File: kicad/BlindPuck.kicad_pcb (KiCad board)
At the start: 2 copper layers, 30.5 x 50.8 mm, 9 parts, among them Q1 FQP30N06, U1 PK-21N30P-TPQ, U2 DD06AJSA, U3 PK-21N30P-TPQ, U4 FeatherHuzzah, U5 InductiveCoil, U6 MPU-6050

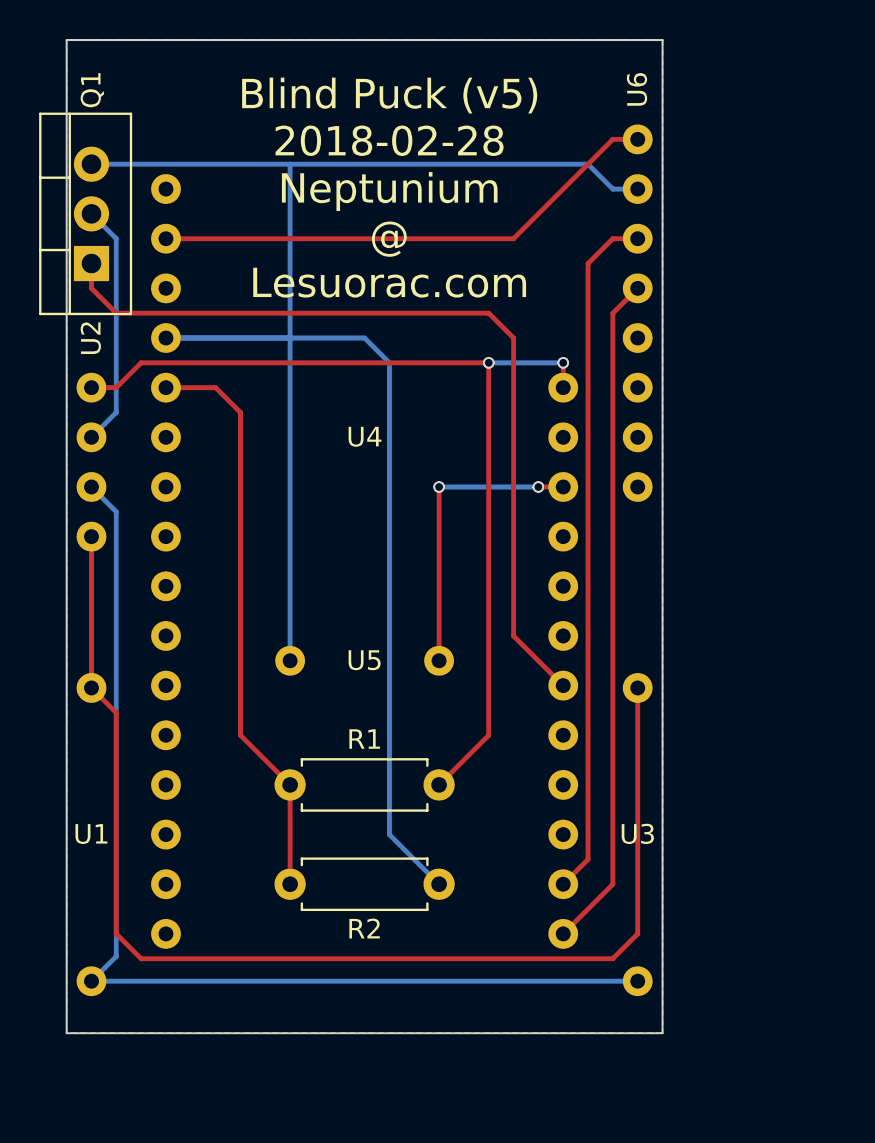
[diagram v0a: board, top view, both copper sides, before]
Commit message: fixed problems where the pcb's hole was too small
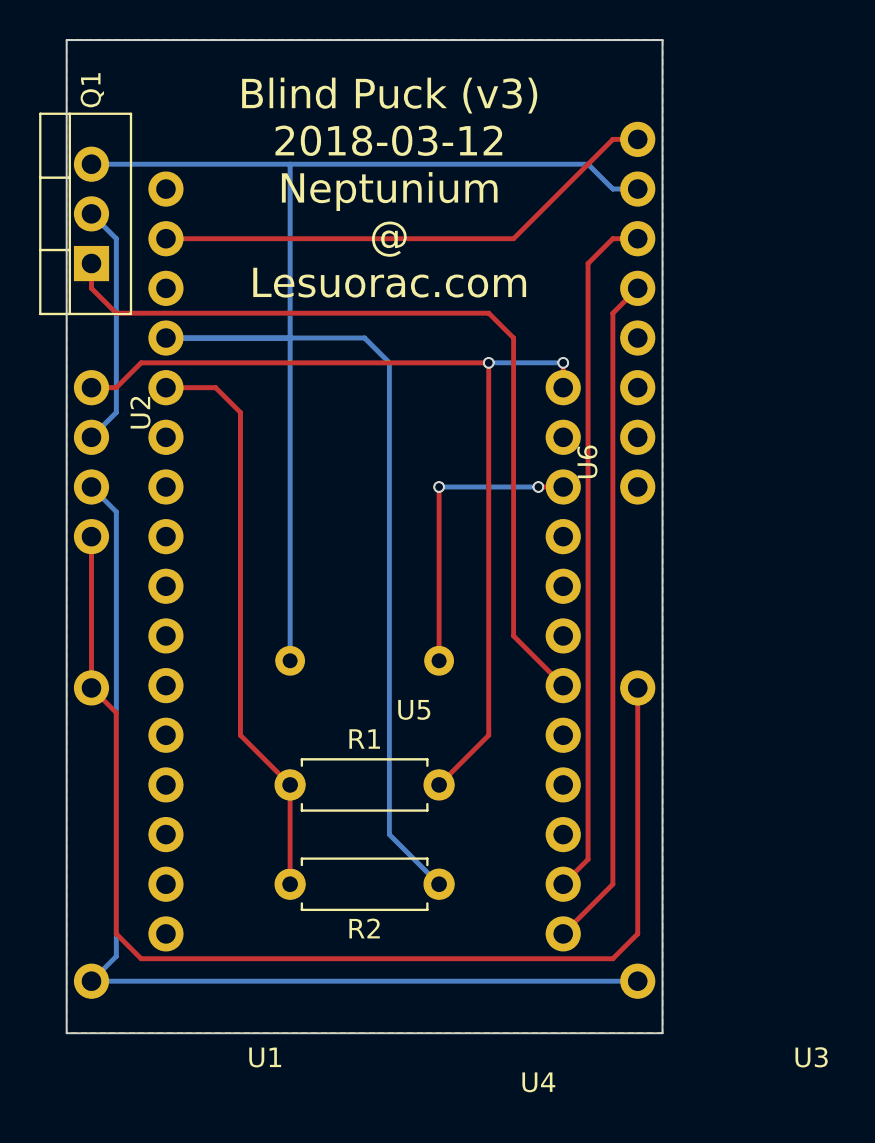
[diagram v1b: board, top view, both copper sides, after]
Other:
- board text added: "+"
- board text added: "-"
- board text added: "Blind Puck (v3) 2018-03-12 Neptunium @ Lesuorac.com"
- board text removed: "Blind Puck (v5) 2018-02-28 Neptunium @ Lesuorac.com"
